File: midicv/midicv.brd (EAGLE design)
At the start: 29.2 x 188.3 mm, 33 parts, among them IC1 OPA2134P, J1 UBBS-4R-D14-4D, X1 2516-

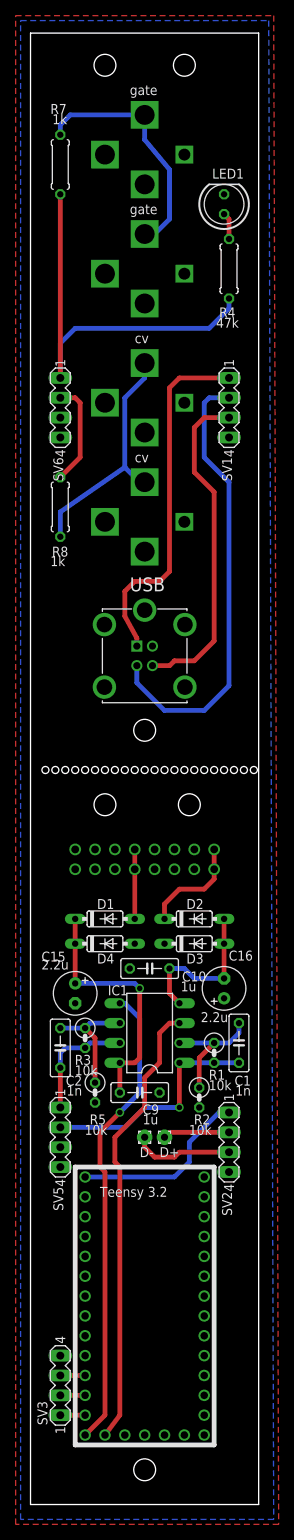
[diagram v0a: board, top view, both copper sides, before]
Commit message: fixed usb polatiry on midicv.  moved holes
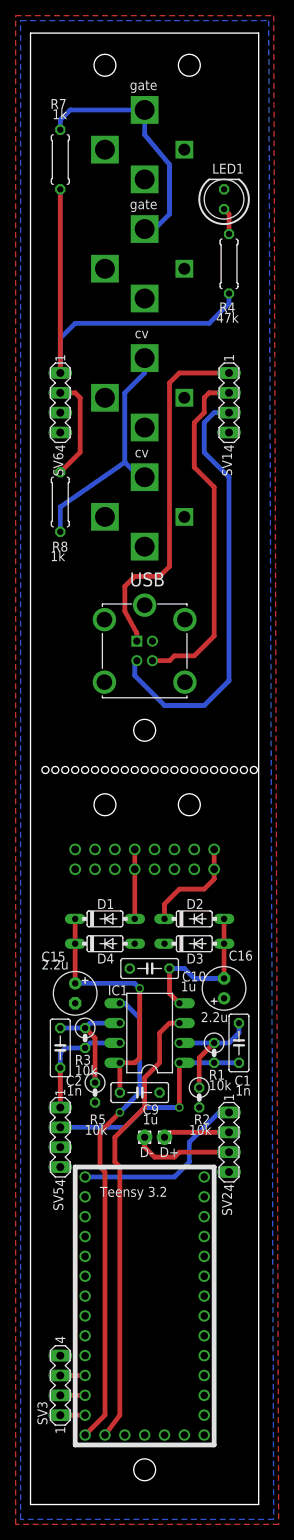
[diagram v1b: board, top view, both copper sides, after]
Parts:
- moved GATE1 0.64 mm to (14.6, 158.1)
- moved R7 0.64 mm to (3.81, 172.1)
- moved J1 0.64 mm to (14.6, 109.2)
- moved R8 0.64 mm to (3.81, 128.3)
- moved CV 0.63 mm to (14.6, 141.6)
- moved CV1 0.63 mm to (14.6, 126.4)
- moved GATE 0.63 mm to (14.6, 173.4)
- moved LED1 0.63 mm to (24.8, 167.0)
- moved R4 0.63 mm to (25.4, 158.8)
- moved SV1 0.63 mm to (25.4, 141.0)
- moved SV6 0.63 mm to (3.81, 141.0)
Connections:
- removed net N$9: J1.2, SV1.2
- new net N$18: J1.2, SV1.3
- net N$11: now also SV1.2; no longer SV1.3
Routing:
- net N$9: track 57.7 -> 0.00 mm
- net N$18: track 0.00 -> 55.0 mm
- net N$11: track 42.5 -> 44.7 mm
